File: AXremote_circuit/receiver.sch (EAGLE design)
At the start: 69 parts, among them Q1 16MHz, Q3 MOSFET-NCHANNELBSS138, Q5 BC849SMD, U1 AX8052F143HS, X1 MINI-USB-SCHIELD-32005-201

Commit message: Started routing receiver rev2.
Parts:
- U$2: value FT121 -> FT121FTDI; device sam:FT121 -> sam:FT121FTDI
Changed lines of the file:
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@@
 <grid distance="0.1" unitdist="inch" unit="inch" style="lines" multiple="1" display="no" altdistance="0.01" altunitdist="inch" altunit="inch"/>
 <layers>
-<layer number="1" name="Top" color="4" fill="1" visible="no" active="no"/>
-<layer number="2" name="Route2" color="1" fill="3" visible="no" active="no"/>
-<layer number="3" name="Route3" color="4" fill="3" visible="no" active="no"/>
-<layer number="4" name="Route4" color="1" fill="4" visible="no" active="no"/>
-<layer number="5" name="Route5" color="4" fill="4" visible="no" active="no"/>
-<layer number="6" name="Route6" color="1" fill="8" visible="no" active="no"/>
-<layer number="7" name="Route7" color="4" fill="8" visible="no" active="no"/>
-<layer number="8" name="Route8" color="1" fill="2" visible="no" active="no"/>
-<layer number="9" name="Route9" color="4" fill="2" visible="no" active="no"/>
-<layer number="10" name="Route10" color="1" fill="7" visible="no" active="no"/>
-<layer number="11" name="Route11" color="4" fill="7" visible="no" active="no"/>
-<layer number="12" name="Route12" color="1" fill="5" visible="no" active="no"/>
-<layer number="13" name="Route13" color="4" fill="5" visible="no" active="no"/>
-<layer number="14" name="Route14" color="1" fill="6" visible="no" active="no"/>
-<layer number="15" name="Route15" color="4" fill="6" visible="no" active="no"/>
-<layer number="16" name="Bottom" color="1" fill="1" visible="no" active="no"/>
-<layer number="17" name="Pads" color="2" fill="1" visible="no" active="no"/>
-<layer number="18" name="Vias" color="2" fill="1" visible="no" active="no"/>
-<layer number="19" name="Unrouted" color="6" fill="1" visible="no" active="no"/>
-<layer number="20" name="Dimension" color="15" fill="1" visible="no" active="no"/>
-<layer number="21" name="tPlace" color="7" fill="1" visible="no" active="no"/>
-<layer number="22" name="bPlace" color="7" fill="1" visible="no" active="no"/>
-<layer number="23" name="tOrigins" color="15" fill="1" visible="no" active="no"/>
-<layer number="24" name="bOrigins" color="15" fill="1" visible="no" active="no"/>
-<layer number="25" name="tNames" color="7" fill="1" visible="no" active="no"/>
-<layer number="26" name="bNames" color="7" fill="1" visible="no" active="no"/>
-<layer number="27" name="tValues" color="7" fill="1" visible="no" active="no"/>
-<layer number="28" name="bValues" color="7" fill="1" visible="no" active="no"/>
+<layer number="1" name="Top" color="4" fill="1" visible="yes" active="no"/>
+<layer number="2" name="Route2" color="1" fill="3" visible="yes" active="no"/>
+<layer number="3" name="Route3" color="4" fill="3" visible="yes" active="no"/>
+<layer number="4" name="Route4" color="1" fill="4" visible="yes" active="no"/>
+<layer number="5" name="Route5" color="4" fill="4" visible="yes" active="no"/>
+<layer number="6" name="Route6" color="1" fill="8" visible="yes" active="no"/>
+<layer number="7" name="Route7" color="4" fill="8" visible="yes" active="no"/>
+<layer number="8" name="Route8" color="1" fill="2" visible="yes" active="no"/>
+<layer number="9" name="Route9" color="4" fill="2" visible="yes" active="no"/>
+<layer number="10" name="Route10" color="1" fill="7" visible="yes" active="no"/>
+<layer number="11" name="Route11" color="4" fill="7" visible="yes" active="no"/>
+<layer number="12" name="Route12" color="1" fill="5" visible="yes" active="no"/>
+<layer number="13" name="Route13" color="4" fill="5" visible="yes" active="no"/>
+<layer number="14" name="Route14" color="1" fill="6" visible="yes" active="no"/>
+<layer number="15" name="Route15" color="4" fill="6" visible="yes" active="no"/>
+<layer number="16" name="Bottom" color="1" fill="1" visible="yes" active="no"/>
+<layer number="17" name="Pads" color="2" fill="1" visible="yes" active="no"/>
+<layer number="18" name="Vias" color="2" fill="1" visible="yes" active="no"/>
+<layer number="19" name="Unrouted" color="6" fill="1" visible="yes" active="no"/>
+<layer number="20" name="Dimension" color="15" fill="1" visible="yes" active="no"/>
+<layer number="21" name="tPlace" color="7" fill="1" visible="yes" active="no"/>
+<layer number="22" name="bPlace" color="7" fill="1" visible="yes" active="no"/>
+<layer number="23" name="tOrigins" color="15" fill="1" visible="yes" active="no"/>
+<layer number="24" name="bOrigins" color="15" fill="1" visible="yes" active="no"/>
+<layer number="25" name="tNames" color="7" fill="1" visible="yes" active="no"/>
+<layer number="26" name="bNames" color="7" fill="1" visible="yes" active="no"/>
+<layer number="27" name="tValues" color="7" fill="1" visible="yes" active="no"/>
+<layer number="28" name="bValues" color="7" fill="1" visible="yes" active="no"/>
 <layer number="29" name="tStop" color="7" fill="3" visible="no" active="no"/>
 <layer number="30" name="bStop" color="7" fill="6" visible="no" active="no"/>
@@
 <layer number="35" name="tGlue" color="7" fill="4" visible="no" active="no"/>
 <layer number="36" name="bGlue" color="7" fill="5" visible="no" active="no"/>
-<layer number="37" name="tTest" color="7" fill="1" visible="no" active="no"/>
-<layer number="38" name="bTest" color="7" fill="1" visible="no" active="no"/>
+<layer number="37" name="tTest" color="7" fill="1" visible="yes" active="no"/>
+<layer number="38" name="bTest" color="7" fill="1" visible="yes" active="no"/>
 <layer number="39" name="tKeepout" color="4" fill="11" visible="no" active="no"/>
 <layer number="40" name="bKeepout" color="1" fill="11" visible="no" active="no"/>
@@
 <layer number="44" name="Drills" color="7" fill="1" visible="no" active="no"/>
 <layer number="45" name="Holes" color="7" fill="1" visible="no" active="no"/>
-<layer number="46" name="Milling" color="3" fill="1" visible="no" active="no"/>
-<layer number="47" name="Measures" color="7" fill="1" visible="no" active="no"/>
-<layer number="48" name="Document" color="7" fill="1" visible="no" active="no"/>
-<layer number="49" name="Reference" color="7" fill="1" visible="no" active="no"/>
-<layer number="50" name="dxf" color="7" fill="1" visible="no" active="no"/>
-<layer number="51" name="tDocu" color="7" fill="1" visible="no" active="no"/>
-<layer number="52" name="bDocu" color="7" fill="1" visible="no" active="no"/>
-<layer number="53" name="tGND_GNDA" color="7" fill="9" visible="no" active="no"/>
-<layer number="54" name="bGND_GNDA" color="1" fill="9" visible="no" active="no"/>
-<layer number="56" name="wert" color="7" fill="1" visible="no" active="no"/>
+<layer number="46" name="Milling" color="3" fill="1" visible="yes" active="no"/>
+<layer number="47" name="Measures" color="7" fill="1" visible="yes" active="no"/>
+<layer number="48" name="Document" color="7" fill="1" visible="yes" active="no"/>
+<layer number="49" name="Reference" color="7" fill="1" visible="yes" active="no"/>
+<layer number="50" name="dxf" color="7" fill="1" visible="yes" active="no"/>
+<layer number="51" name="tDocu" color="7" fill="1" visible="yes" active="no"/>
+<layer number="52" name="bDocu" color="7" fill="1" visible="yes" active="no"/>
+<layer number="53" name="tGND_GNDA" color="7" fill="9" visible="yes" active="no"/>
+<layer number="54" name="bGND_GNDA" color="1" fill="9" visible="yes" active="no"/>
+<layer number="56" name="wert" color="7" fill="1" visible="yes" active="no"/>
 <layer number="91" name="Nets" color="2" fill="1" visible="yes" active="yes"/>
 <layer number="92" name="Busses" color="1" fill="1" visible="yes" active="yes"/>
@@
 <part name="GND42" library="supply1" deviceset="GND" device=""/>
 <part name="U$7" library="sam" deviceset="SWITCH" device="SMD"/>
-<part name="U$2" library="sam" deviceset="FT121" device=""/>
+<part name="U$2" library="sam" deviceset="FT121" device="FTDI" value="FT121FTDI"/>
 <part name="BEAD" library="resistor" deviceset="R-EU_" device="R0603" value="ferrite"/>
 <part name="C12" library="resistor" deviceset="C-EU" device="C0603K" value="47pF"/>

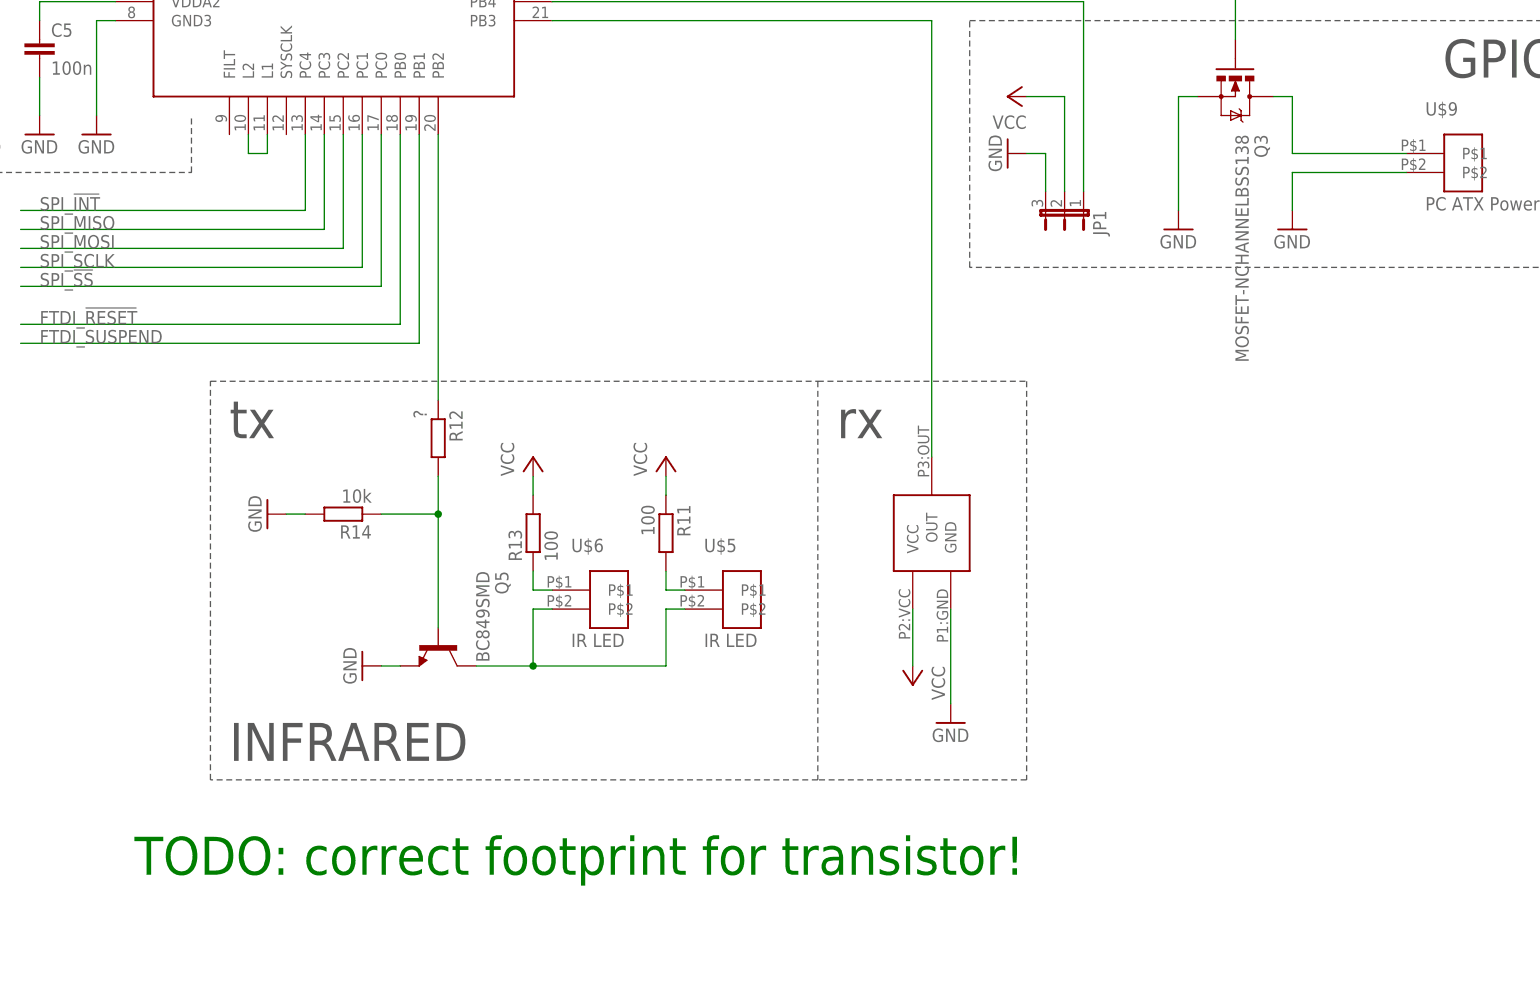
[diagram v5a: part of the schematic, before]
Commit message: Routed receiver rev2.
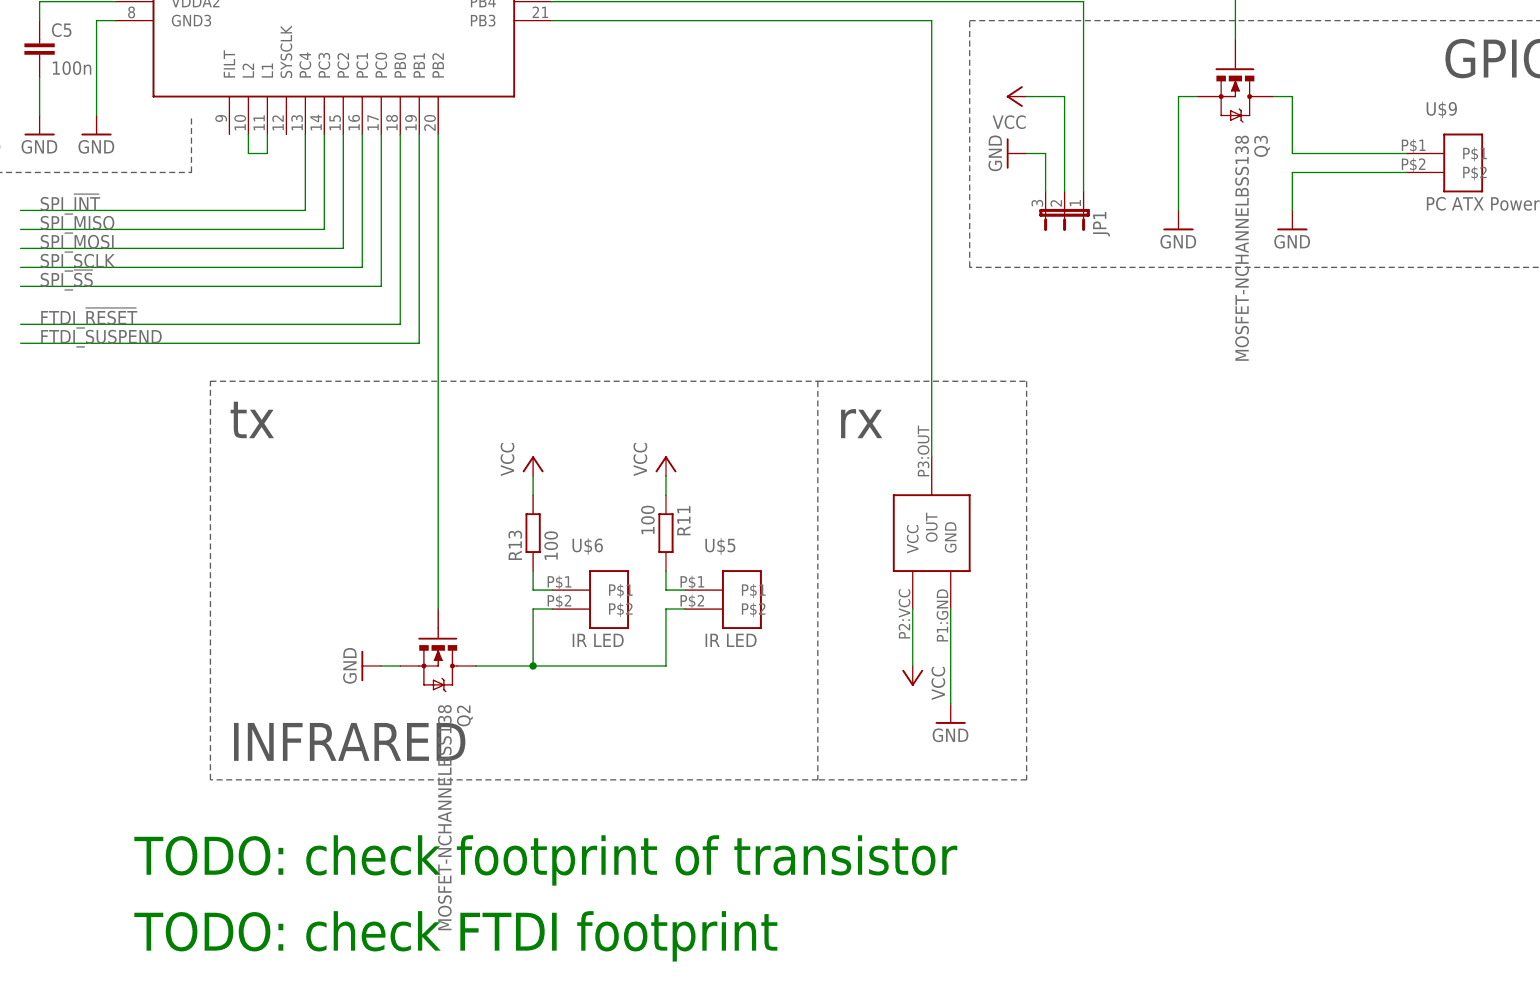
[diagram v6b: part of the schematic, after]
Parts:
- removed Q5: BC849SMD, transistor-npn:BC849SMD
- removed R12: ?, resistor:R-EU_R0603
- removed R14: 10k, resistor:R-EU_R0603
- added Q2: MOSFET-NCHANNELBSS138, SparkFun-DiscreteSemi:MOSFET-NCHANNELBSS138
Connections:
- removed net N$43: Q5.B, R12.2, R14.1
- net GND: now also Q2.S; no longer Q5.E, R14.2
- net N$41: now also Q2.D; no longer Q5.C
- net N$42: now also Q2.G; no longer R12.1
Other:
- note added: "TODO: check FTDI footprint"
- note added: "TODO: check footprint of transistor"
- note removed: "TODO: correct footprint for transistor!"

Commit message: working on IR
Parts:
- R15, R18: value 100 -> 10k
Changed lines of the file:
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@@
 <part name="R17" library="resistor" deviceset="R-EU_" device="R0603" value="10k"/>
 <part name="P+10" library="supply1" deviceset="VCC" device=""/>
-<part name="R18" library="resistor" deviceset="R-EU_" device="R0603" value="100"/>
+<part name="R18" library="resistor" deviceset="R-EU_" device="R0603" value="10k"/>
 <part name="GND48" library="supply1" deviceset="GND" device=""/>
 <part name="R11" library="resistor" deviceset="R-EU_" device="R0603" value="100"/>
@@
 <part name="U$10" library="sam" deviceset="SWITCH" device="SMD"/>
 <part name="P+12" library="supply1" deviceset="VCC" device=""/>
-<part name="R15" library="resistor" deviceset="R-EU_" device="R0603" value="100"/>
+<part name="R15" library="resistor" deviceset="R-EU_" device="R0603" value="10k"/>
 <part name="GND11" library="supply1" deviceset="GND" device=""/>
 <part name="JP1" library="jumper" deviceset="JP2E" device=""/>
